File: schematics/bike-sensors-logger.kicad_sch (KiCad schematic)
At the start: 7 parts, among them J1 MMCX, J2 OBD II

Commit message: Micro SD
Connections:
- net Micro SD/DAT0: now reaches A1.D10 (D10_SS)
- net Micro SD/MOSI: now reaches A1.D11 (D11_MOSI)
- net Micro SD/MISO: now reaches A1.D12 (D12_MISO)
- net Micro SD/CLK: now reaches A1.D13 (D13_SCK)
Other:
- added sheet Micro SD (micro-sd.kicad_sch)
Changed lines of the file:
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@@
 	(title_block
 		(title "Bike sensors logger MK1")
+		(comment 1 "It will probably require a 5-to-3.3V buck from the main 5V buck instead")
+		(comment 2 "TODO: check overall current consumption on 3V3 port.")
+	)
+	(junction
+		(at 93.98 81.28)
+		(diameter 0)
+		(color 0 0 0 0)
 	)
 	(junction
@@
 	)
 	(junction
+		(at 180.34 68.58)
+		(diameter 0)
+		(color 0 0 0 0)
+	)
+	(junction
 		(at 105.41 81.28)
 		(diameter 0)
@@
 	(wire
 		(pts
+			(xy 93.98 132.08) (xy 163.83 132.08)
+		)
+		(stroke
+			(width 0)
+			(type default)
+		)
+	)
+	(wire
+		(pts
 			(xy 90.17 35.56) (xy 90.17 59.69)
 		)
@@
 	(wire
 		(pts
+			(xy 180.34 68.58) (xy 182.88 68.58)
+		)
+		(stroke
+			(width 0)
+			(type default)
+		)
+	)
+	(wire
+		(pts
 			(xy 163.83 20.32) (xy 163.83 45.72)
 		)
@@
 	(wire
 		(pts
+			(xy 93.98 81.28) (xy 93.98 132.08)
+		)
+		(stroke
+			(width 0)
+			(type default)
+		)
+	)
+	(wire
+		(pts
 			(xy 104.14 97.79) (xy 160.02 97.79)
 		)
@@
 	(wire
 		(pts
+			(xy 158.75 68.58) (xy 180.34 68.58)
+		)
+		(stroke
+			(width 0)
+			(type default)
+		)
+	)
+	(wire
+		(pts
 			(xy 73.66 96.52) (xy 102.87 96.52)
 		)
@@
 	(wire
 		(pts
-			(xy 78.74 81.28) (xy 101.6 81.28)
+			(xy 78.74 81.28) (xy 93.98 81.28)
 		)
 		(stroke
@@
 	(wire
 		(pts
+			(xy 182.88 58.42) (xy 180.34 58.42)
+		)
+		(stroke
+			(width 0)
+			(type default)
+		)
+	)
+	(wire
+		(pts
+			(xy 180.34 58.42) (xy 180.34 68.58)
+		)
+		(stroke
+			(width 0)
+			(type default)
+		)
+	)
+	(wire
+		(pts
 			(xy 168.91 50.8) (xy 168.91 29.21)
 		)
@@
 	(wire
 		(pts
+			(xy 158.75 66.04) (xy 182.88 66.04)
+		)
+		(stroke
+			(width 0)
+			(type default)
+		)
+	)
+	(wire
+		(pts
 			(xy 87.63 35.56) (xy 90.17 35.56)
 		)
@@
 	(wire
 		(pts
+			(xy 163.83 132.08) (xy 163.83 73.66)
+		)
+		(stroke
+			(width 0)
+			(type default)
+		)
+	)
+	(wire
+		(pts
 			(xy 158.75 53.34) (xy 171.45 53.34)
 		)
@@
 	(wire
 		(pts
+			(xy 158.75 60.96) (xy 182.88 60.96)
+		)
+		(stroke
+			(width 0)
+			(type default)
+		)
+	)
+	(wire
+		(pts
 			(xy 25.4 54.61) (xy 24.13 54.61)
 		)
@@
 	(wire
 		(pts
+			(xy 93.98 81.28) (xy 101.6 81.28)
+		)
+		(stroke
+			(width 0)
+			(type default)
+		)
+	)
+	(wire
+		(pts
 			(xy 81.28 116.84) (xy 102.87 116.84)
 		)
@@
 		(pts
 			(xy 24.13 54.61) (xy 24.13 17.78)
+		)
+		(stroke
+			(width 0)
+			(type default)
+		)
+	)
+	(wire
+		(pts
+			(xy 158.75 63.5) (xy 182.88 63.5)
+		)
+		(stroke
+			(width 0)
+			(type default)
+		)
+	)
+	(wire
+		(pts
+			(xy 163.83 73.66) (xy 190.5 73.66)
+		)
+		(stroke
+			(width 0)
+			(type default)
+		)
+	)
+	(wire
+		(pts
+			(xy 190.5 71.12) (xy 190.5 73.66)
 		)
 		(stroke
@@
 				)
 			)
+		)
+	)
+	(sheet
+		(at 182.88 55.88)
+		(size 12.7 15.24)
+		(exclude_from_sim no)
+		(in_bom yes)
+		(on_board yes)
+		(dnp no)
+		(fields_autoplaced yes)
+		(stroke
+			(width 0.1524)
+			(type solid)
+		)
+		(fill
+			(color 0 0 0 0.0000)
+		)
+		(property "Sheetname" "Micro SD"
+			(at 182.88 55.1684 0)
+			(effects
+				(font
+					(size 1.27 1.27)
+				)
+				(justify left bottom)
+			)
+		)
+		(property "Sheetfile" "micro-sd.kicad_sch"
+			(at 182.88 71.7046 0)
+			(effects
+				(font
+					(size 1.27 1.27)
+				)
+				(justify left top)
+			)
+		)
+		(pin "CLK" input
+			(at 182.88 68.58 180)
+			(effects
+				(font
+					(size 1.27 1.27)
+				)
+				(justify left)
+			)
+		)
+		(pin "CMD" bidirectional
+			(at 182.88 58.42 180)
+			(effects
+				(font
+					(size 1.27 1.27)
+				)
+				(justify left)
+			)
+		)
+		(pin "DAT0" bidirectional
+			(at 182.88 60.96 180)
+			(effects
+				(font
+					(size 1.27 1.27)
+				)
+				(justify left)
+			)
+		)
+		(pin "MISO" bidirectional
+			(at 182.88 66.04 180)
+			(effects
+				(font
+					(size 1.27 1.27)
+				)
+				(justify left)
+			)
+		)
+		(pin "MOSI" bidirectional
+			(at 182.88 63.5 180)
+			(effects
+				(font
+					(size 1.27 1.27)
+				)
+				(justify left)
+			)
+		)
+		(pin "VDD" input
+			(at 190.5 71.12 270)
+			(effects
+				(font
+					(size 1.27 1.27)
+				)
+				(justify left)
+			)
+		)
+		(instances
+			(project "bike-sensors-logger"
+				(path "/2c1d9222-af16-428b-85a5-a3d420373d70"
+					(page "6")
+				)
+			)

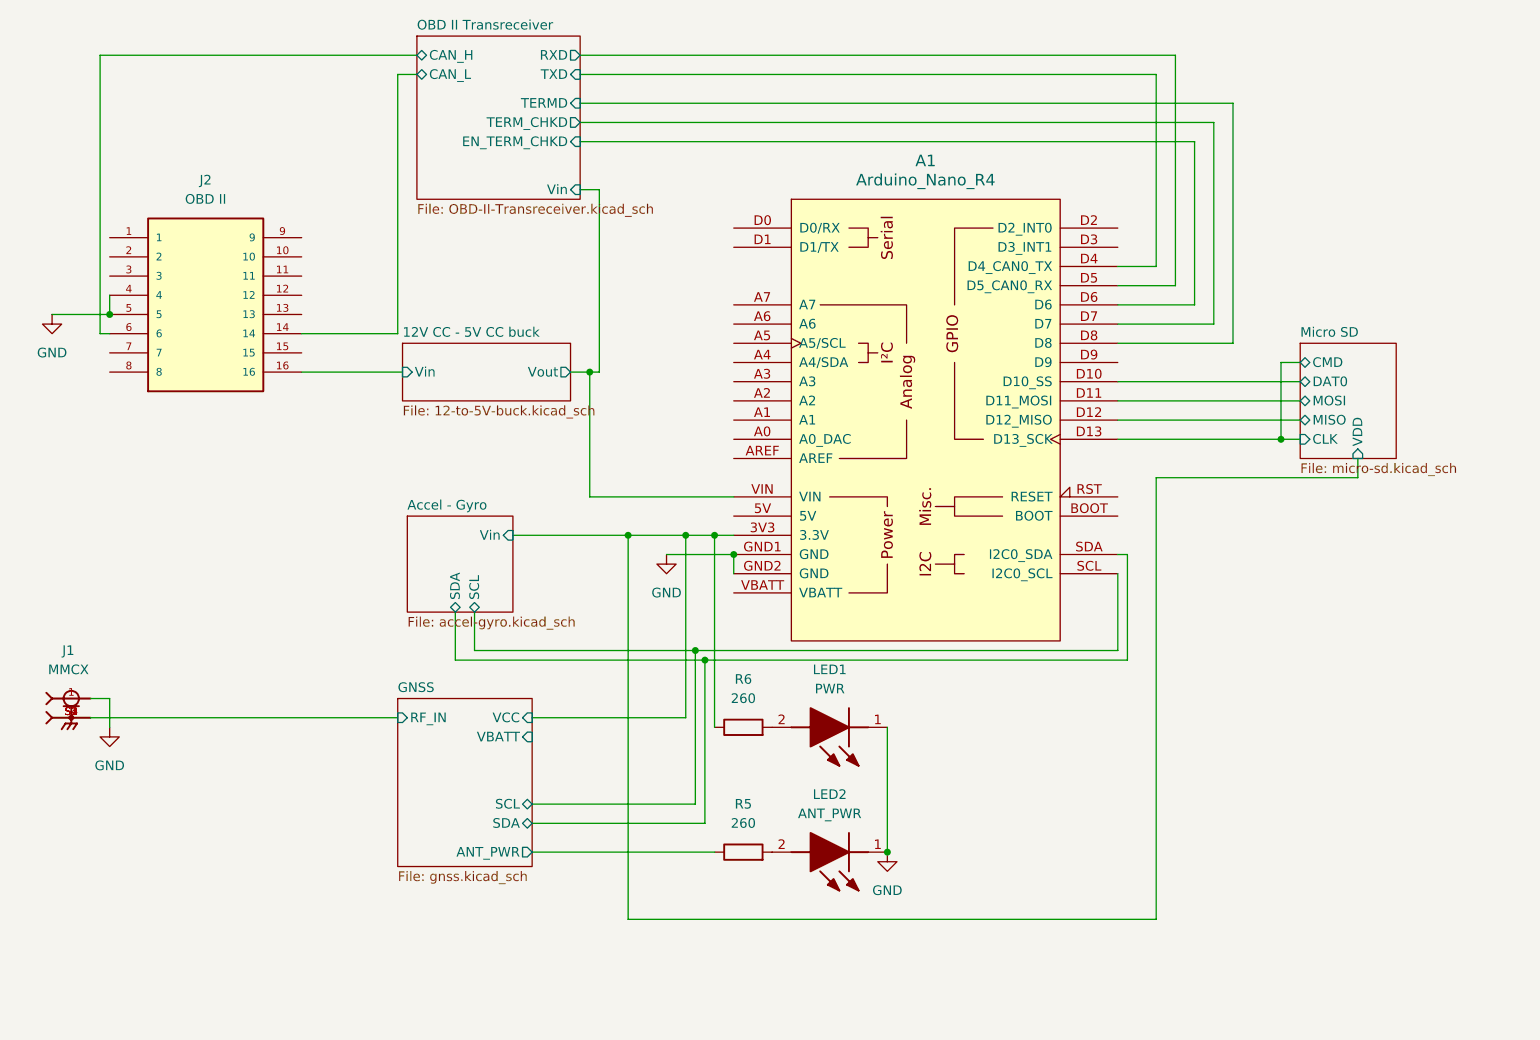
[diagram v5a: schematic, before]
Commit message: Integrated 3V3 buck converter due to Arduino's current limits
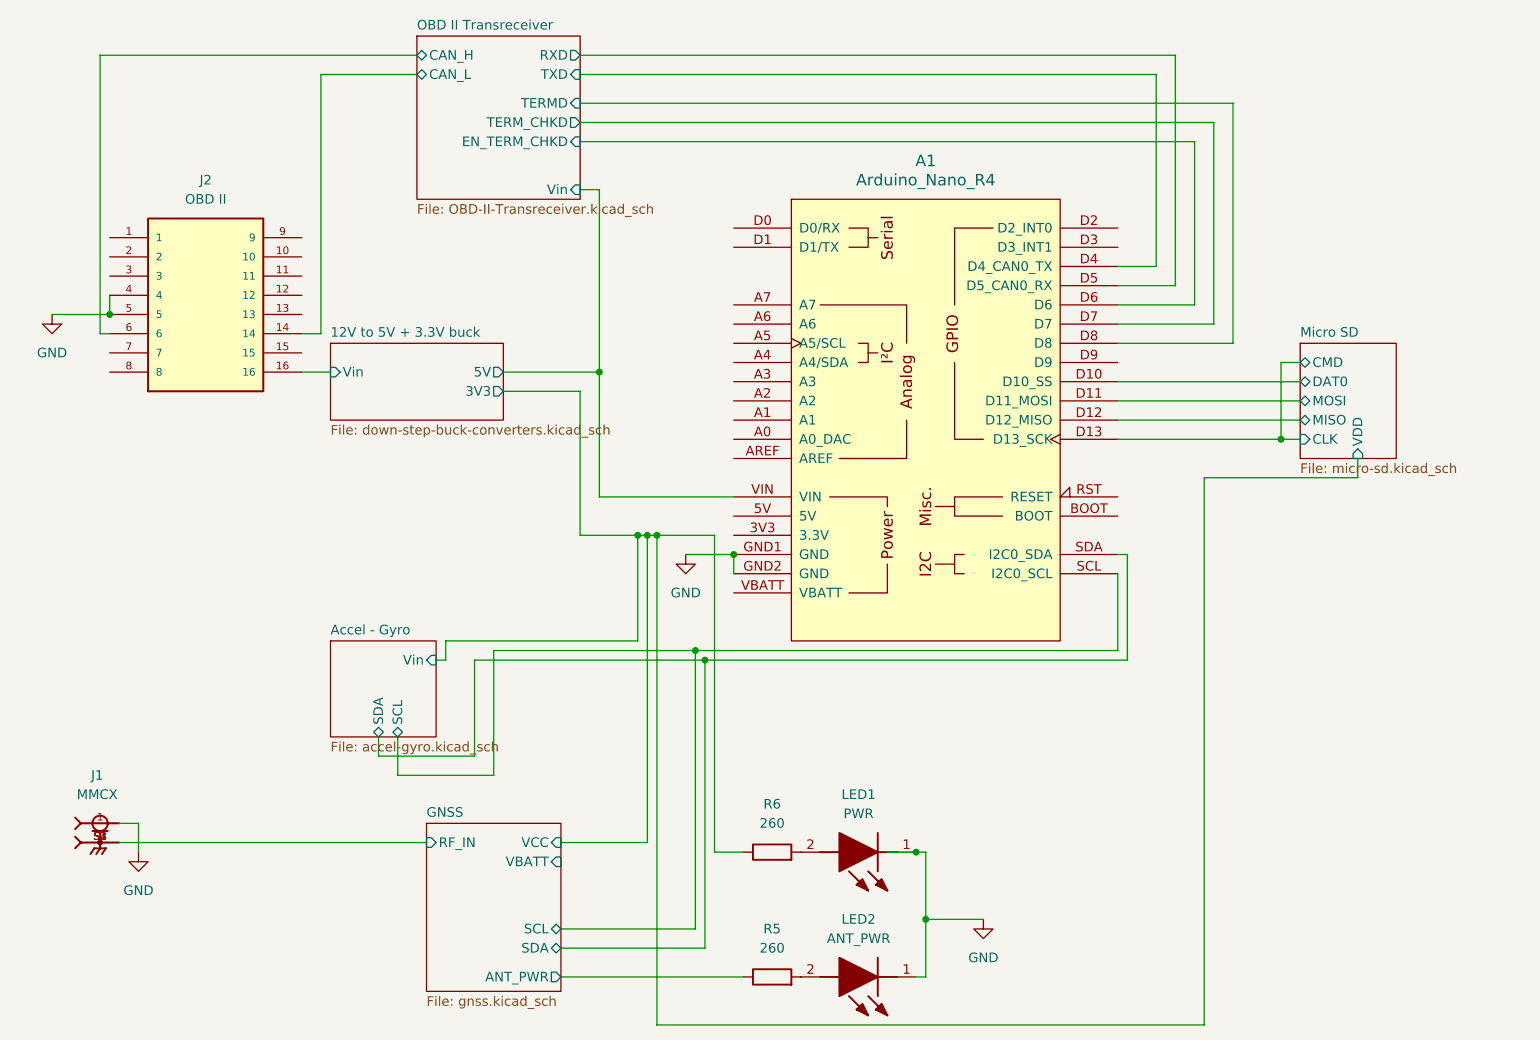
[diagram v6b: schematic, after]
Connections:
- net 12V to 5V + 3.3V buck/Vout renamed 12V to 5V + 3.3V buck/5V
- net Accel - Gyro/Vin: no longer names the net of A1.3V3 (3.3V)
- net Accel - Gyro/Vin: no longer R6.1
- new net 12V to 5V + 3.3V buck/3V3: R6.1
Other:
- sheet 12V CC - 5V CC buck renamed 12V to 5V + 3.3V buck
- sheet 12V to 5V + 3.3V buck: file 12-to-5V-buck.kicad_sch -> down-step-buck-converters.kicad_sch
- sheet 12V to 5V + 3.3V buck ports: added 3V3, 5V; removed Vout
- moved on the sheet: J1, LED1, LED2, R5, R6
